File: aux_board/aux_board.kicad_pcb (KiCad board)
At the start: 4 copper layers, 80 x 80 mm, 111 parts, among them J1 Conn_02x13_Odd_Even, J10 10155435-00011LF, J2 Conn_02x03_Odd_Even, J3 Conn_02x04_Odd_Even, J4 Conn_01x02_Pin, J5 PC104 Conn_02x20_Odd_Even, J6 Conn_01x03_Pin, J7 Conn_01x03_Pin, J8 10155435-00011LF, J9 10155435-00011LF, SW1 EVP-AA602W, SW2 EVP-AA602W, U1 STM32L496RGTx, U2 TJA1042TK-3, U3 TJA1042TK-3, U4 FT230XS, U5 FT230XS, U6 TPS631000DRLR, U7 TPS631000DRLR, U8 TPS631000DRLR, X1 ECS-TXO-2016-33-100-TR

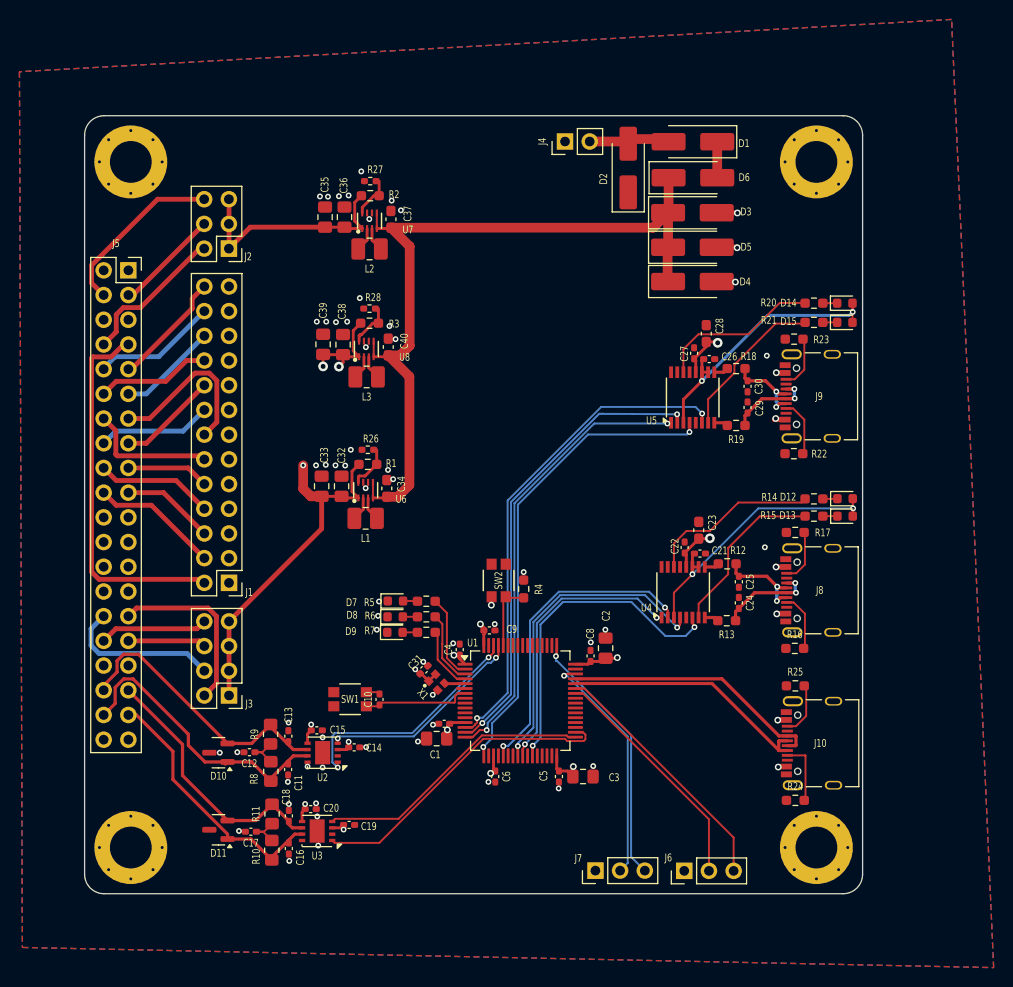
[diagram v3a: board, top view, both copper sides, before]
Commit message: assign can power to core powerm will need to use GPIO to enable power stndby from MCUs, finalize pc104 bus assignments
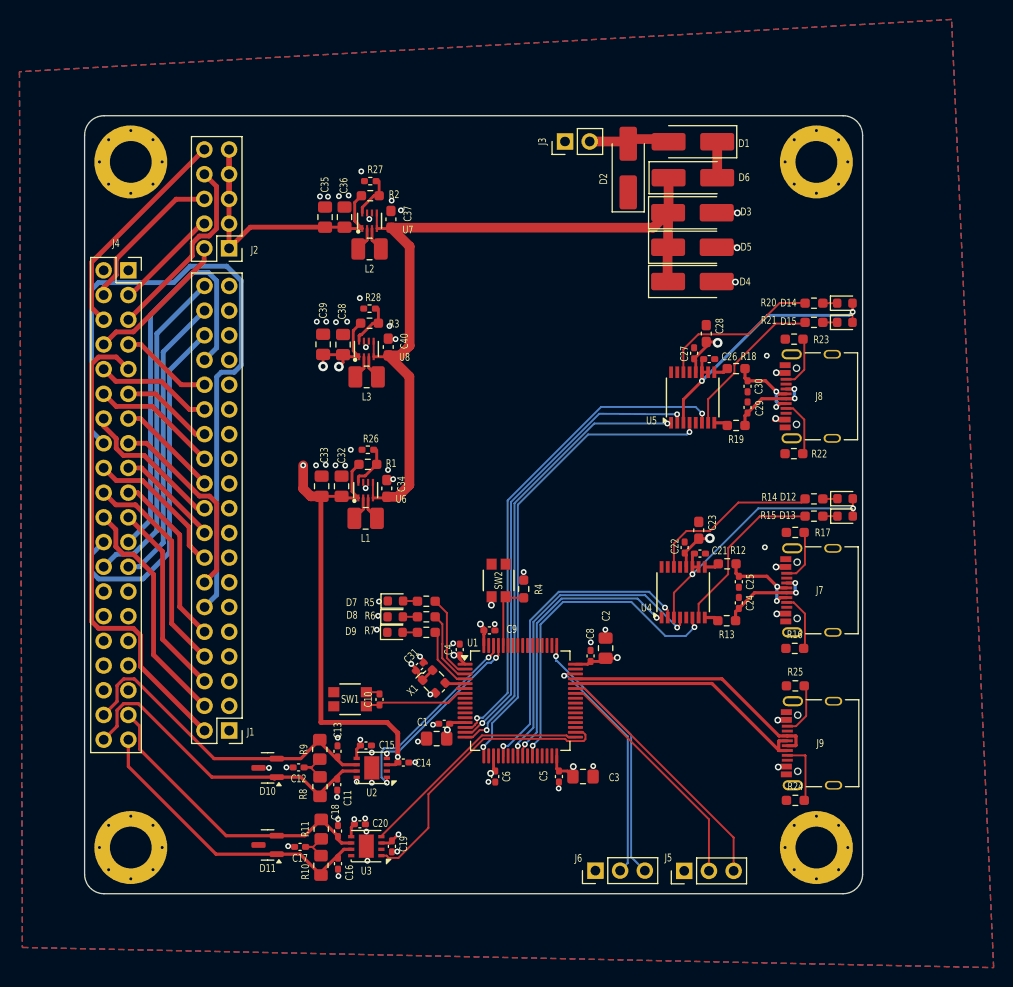
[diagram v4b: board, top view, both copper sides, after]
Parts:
- removed the J3 at (74.8, 119.6)
- J1: footprint Connector_PinHeader_2.54mm:PinHeader_2x13_P2.54mm_Vertical -> Connector_PinHeader_2.54mm:PinHeader_2x19_P2.54mm_Vertical
- J2: value Conn_02x03_Odd_Even -> Conn_02x05_Odd_Even; footprint Connector_PinHeader_2.54mm:PinHeader_2x03_P2.54mm_Vertical -> Connector_PinHeader_2.54mm:PinHeader_2x05_P2.54mm_Vertical
- X1: value ECS-TXO-2016-33-100-TR -> 10MHz; footprint Project:OSC_ECS-1618-300-BN-TR -> Oscillator:Oscillator_SMD_ECS_2520MV-xxx-xx-4Pin_2.5x2.0mm
- moved J1 15.2 mm to (74.9, 123.2)
- moved C11 5.29 mm to (86.0, 128.8)
- moved C14 5.29 mm to (92.8, 126.5)
- moved C15 5.29 mm to (88.9, 124.8)
- moved C16 5.29 mm to (86.1, 136.9)
- moved C17 5.29 mm to (82.2, 135.2)
- moved C18 5.29 mm to (86.1, 133.6)
- moved C20 5.29 mm to (88.3, 132.9)
- moved R10 5.29 mm to (84.3, 137.1)
- moved R9 5.29 mm to (84.2, 125.2)
- moved U2 5.29 mm to (89.5, 127.1)
- moved U3 5.29 mm to (89.0, 135.1)
- moved R8 5.29 mm to (84.2, 129.0)
- moved C12 5.29 mm to (82.0, 127.0)
- moved C13 5.29 mm to (86.0, 125.4)
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- renumbered J4 to J3, J5 to J4, J6 to J5, J7 to J6, J8 to J7, J9 to J8, J10 to J9
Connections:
- net /INTERBOARD_CONNECTOR/BATT_1 renamed /INTERBOARD_CONNECTOR/BATT_1_COMM1_VRF
- net /INTERBOARD_CONNECTOR/BATT_2 renamed /INTERBOARD_CONNECTOR/BATT_2_COMM2_VRF
- J1 pad 10: /INTERBOARD_CONNECTOR/3V3_5 -> /INTERBOARD_CONNECTOR/3V3_5_AVI_ACS_LOGIC
- J1 pad 12: /INTERBOARD_CONNECTOR/3V3_6 -> /INTERBOARD_CONNECTOR/3V3_6_AVI_GYRO
- J1 pad 14: /INTERBOARD_CONNECTOR/3V3_7 -> /INTERBOARD_CONNECTOR/3V3_7_AVI_MAG
- J1 pad 16: /INTERBOARD_CONNECTOR/3V3_8 -> /INTERBOARD_CONNECTOR/3V3_8_AVI_CLK
- J1 pad 18: /INTERBOARD_CONNECTOR/3V3_9 -> /INTERBOARD_CONNECTOR/3V3_9_SCI_STM_CORE
- J1 pad 2: /INTERBOARD_CONNECTOR/3V3_1 -> /INTERBOARD_CONNECTOR/3V3_1_AVI_STM_CORE
- J1 pad 20: /INTERBOARD_CONNECTOR/3V3_10 -> /INTERBOARD_CONNECTOR/3V3_10_SCI_MRAM
- J1 pad 22: /INTERBOARD_CONNECTOR/3V3_11 -> /INTERBOARD_CONNECTOR/3V3_11_SCI_FLASH
- J1 pad 24: /INTERBOARD_CONNECTOR/3V3_12 -> /INTERBOARD_CONNECTOR/3V3_12_SCI_THERMAL
- J1 pad 26: /INTERBOARD_CONNECTOR/3V3_13 -> /INTERBOARD_CONNECTOR/3V3_13_SCI_CAMERAS
- J1 pad 4: /INTERBOARD_CONNECTOR/3V3_2 -> /INTERBOARD_CONNECTOR/3V3_2_AVI_GPS
- J1 pad 6: /INTERBOARD_CONNECTOR/3V3_3 -> /INTERBOARD_CONNECTOR/3V3_3_AVI_MRAM
- J1 pad 8: /INTERBOARD_CONNECTOR/3V3_4 -> /INTERBOARD_CONNECTOR/3V3_4_AVI_SUN
- J4 pad 10: /INTERBOARD_CONNECTOR/3V3_12 -> /INTERBOARD_CONNECTOR/3V3_14_EXTRA1
- J4 pad 11: /INTERBOARD_CONNECTOR/3V3_11 -> /INTERBOARD_CONNECTOR/3V3_13_SCI_CAMERAS
- J4 pad 12: /INTERBOARD_CONNECTOR/3V3_10 -> /INTERBOARD_CONNECTOR/3V3_12_SCI_THERMAL
- J4 pad 13: /INTERBOARD_CONNECTOR/3V3_7 -> /INTERBOARD_CONNECTOR/3V3_11_SCI_FLASH
- J4 pad 14: /INTERBOARD_CONNECTOR/3V3_6 -> /INTERBOARD_CONNECTOR/3V3_10_SCI_MRAM
- J4 pad 15: /INTERBOARD_CONNECTOR/3V3_9 -> /INTERBOARD_CONNECTOR/3V3_7_AVI_MAG
- J4 pad 16: /INTERBOARD_CONNECTOR/3V3_8 -> /INTERBOARD_CONNECTOR/3V3_6_AVI_GYRO
- J4 pad 17: /INTERBOARD_CONNECTOR/3V3_5 -> /INTERBOARD_CONNECTOR/3V3_9_SCI_STM_CORE
- J4 pad 18: /INTERBOARD_CONNECTOR/3V3_4 -> /INTERBOARD_CONNECTOR/3V3_8_AVI_CLK
- J4 pad 19: /INTERBOARD_CONNECTOR/3V3_3 -> /INTERBOARD_CONNECTOR/3V3_5_AVI_ACS_LOGIC
- J4 pad 20: /INTERBOARD_CONNECTOR/3V3_2 -> /INTERBOARD_CONNECTOR/3V3_4_AVI_SUN
- J4 pad 21: /INTERBOARD_CONNECTOR/*ATTENTION -> /INTERBOARD_CONNECTOR/3V3_3_AVI_MRAM
- J4 pad 22: /INTERBOARD_CONNECTOR/*EPS_RST -> /INTERBOARD_CONNECTOR/3V3_2_AVI_GPS
- J4 pad 23: /INTERBOARD_CONNECTOR/*SCI_RST -> /INTERBOARD_CONNECTOR/3V3_17_RF1_BRIDGE
- J4 pad 24: /INTERBOARD_CONNECTOR/*AVI_RST -> /INTERBOARD_CONNECTOR/3V3_18_RF1_COMM
- J4 pad 25: /INTERBOARD_CONNECTOR/*COMM1_RST -> /INTERBOARD_CONNECTOR/3V3_19_RF2_BRIDGE
- J4 pad 26: /INTERBOARD_CONNECTOR/*COMM2_RST -> /INTERBOARD_CONNECTOR/3V3_20_RF2_COMM
- J4 pad 29: /INTERBOARD_CONNECTOR/5V0_1 -> /INTERBOARD_CONNECTOR/*ATTENTION
- J4 pad 30: /INTERBOARD_CONNECTOR/5V0_2 -> /INTERBOARD_CONNECTOR/*EPS_RST
- J4 pad 31: /INTERBOARD_CONNECTOR/5V0_3 -> /INTERBOARD_CONNECTOR/*SCI_RST
- J4 pad 32: /INTERBOARD_CONNECTOR/5V0_4 -> /INTERBOARD_CONNECTOR/*AVI_RST
- J4 pad 33: GND -> /INTERBOARD_CONNECTOR/*COMM1_RST
- J4 pad 34: GND -> /INTERBOARD_CONNECTOR/*COMM2_RST
- J4 pad 35: /CAN2_L -> GND
- J4 pad 36: /CAN1_L -> GND
- J4 pad 37: /CAN2_H -> /CAN2_L
- J4 pad 38: /CAN1_H -> /CAN1_L
- J4 pad 39: GND -> /CAN2_H
- J4 pad 40: GND -> /CAN1_H
- J4 pad 5: GND -> /INTERBOARD_CONNECTOR/BATT_3_AVI_ACS_COIL
- J4 pad 6: GND -> /INTERBOARD_CONNECTOR/BATT_4_SCI_CAMERAS
- J4 pad 7: /INTERBOARD_CONNECTOR/3V3_1 -> /INTERBOARD_CONNECTOR/3V3_15_EXTRA2
- J4 pad 9: /INTERBOARD_CONNECTOR/3V3_13 -> /INTERBOARD_CONNECTOR/3V3_1_AVI_STM_CORE
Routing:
- net /INTERBOARD_CONNECTOR/3V3_6_AVI_GYRO: track 0.00 -> 69.2 mm
- net /INTERBOARD_CONNECTOR/3V3_1_AVI_STM_CORE: track 0.00 -> 49.2 mm
- net /INTERBOARD_CONNECTOR/3V3_17_RF1_BRIDGE: track 0.00 -> 41.9 mm
- net /INTERBOARD_CONNECTOR/3V3_1: track 38.4 -> 0.00 mm
- net /INTERBOARD_CONNECTOR/3V3_18_RF1_COMM: track 0.00 -> 36.8 mm
- net /INTERBOARD_CONNECTOR/3V3_20_RF2_COMM: track 0.00 -> 34.2 mm
- net /INTERBOARD_CONNECTOR/3V3_19_RF2_BRIDGE: track 0.00 -> 30.2 mm
- net /INTERBOARD_CONNECTOR/3V3_2_AVI_GPS: track 0.00 -> 24.3 mm
- net /INTERBOARD_CONNECTOR/BATT_4_SCI_CAMERAS: track 0.00 -> 22.8 mm
- net /INTERBOARD_CONNECTOR/3V3_4_AVI_SUN: track 0.00 -> 22.3 mm
- net /INTERBOARD_CONNECTOR/3V3_7_AVI_MAG: track 0.00 -> 20.3 mm
- net /INTERBOARD_CONNECTOR/3V3_3_AVI_MRAM: track 0.00 -> 20.1 mm
- net /INTERBOARD_CONNECTOR/BATT_3_AVI_ACS_COIL: track 0.00 -> 19.8 mm
- net /INTERBOARD_CONNECTOR/5V0_1: track 18.4 -> 0.00 mm
- net /INTERBOARD_CONNECTOR/3V3_5_AVI_ACS_LOGIC: track 0.00 -> 18.1 mm
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
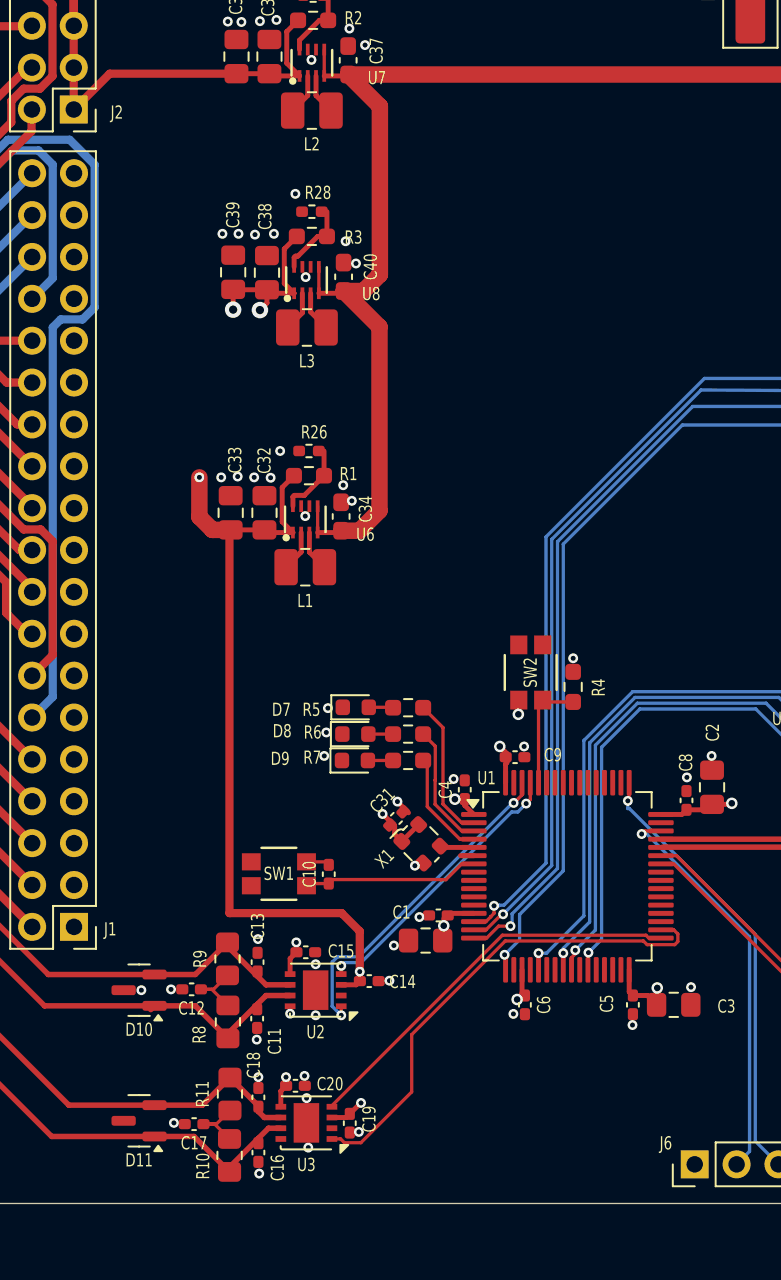
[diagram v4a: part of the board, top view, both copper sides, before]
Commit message: replacd TJA1042 with TCAN3414 that allows differential from 3V, negating the need for 5V generator
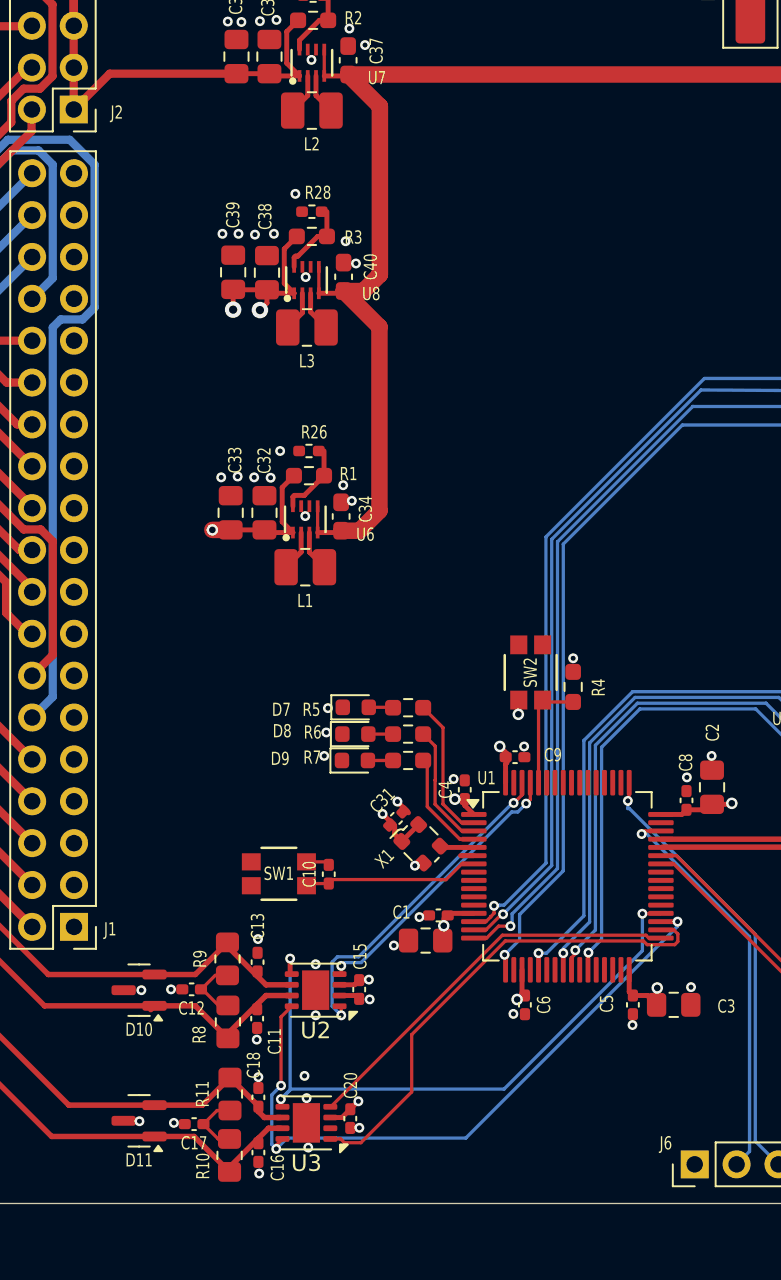
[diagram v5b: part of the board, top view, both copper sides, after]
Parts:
- removed C14, C19: 100n, Capacitor_SMD:C_0402_1005Metric_Pad0.74x0.62mm_HandSolder
- U2, U3: value TJA1042TK-3 -> TCAN3414; footprint Package_DFN_QFN:DFN-8-1EP_3x3mm_P0.65mm_EP1.55x2.4mm -> Package_SON:VSON-8-1EP_3x3mm_P0.65mm_EP1.65x2.4mm
- moved C15 3.95 mm to (92.2, 127.0), turned to -90 degrees
- moved C20 3.88 mm to (91.6, 134.8), turned to -90 degrees
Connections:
- U1 pad 35: unconnected-(U1-PB14-Pad35) -> /CAN TO USB/CAN_STB
- U1 pad 36: unconnected-(U1-PB15-Pad36) -> /CAN TO USB/CAN_SHTD
- U2 pad 3: +5V -> +3V3
- U2 pad 5: +3V3 -> /CAN TO USB/CAN_SHTD
- U2 pad 8: GND -> /CAN TO USB/CAN_STB
- U3 pad 3: +5V -> +3V3
- U3 pad 5: +3V3 -> /CAN TO USB/CAN_SHTD
- U3 pad 8: GND -> /CAN TO USB/CAN_STB
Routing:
- net +5V: track 139.8 -> 93.6 mm, vias 5 -> 3
- net /CAN TO USB/CAN_STB: track 0.00 -> 41.3 mm, vias 0 -> 3
- net /CAN TO USB/CAN_SHTD: track 0.00 -> 39.2 mm, vias 0 -> 3
- net +3V3: track 36.8 -> 44.6 mm
- net GND: track 3.73 -> 5.00 mm
